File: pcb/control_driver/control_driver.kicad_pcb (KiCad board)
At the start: 2 copper layers, 60 parts, among them P1 CONN_2, P2 CONN_4, P3 CONN_2, P4 CONN_4, P5 CONN_4, P6 CONN_4, P7 CONN_4, Q1 MOSFET_N, Q2 MOSFET_N, Q3 MOSFET_N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

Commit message: control/driver PCB arranged
All the components for the control/driver PCB have
been arranged.  Next traces need to be added.
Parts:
- moved P7 485.1 mm to (251.5, 203.2)
- moved P6 462.2 mm to (231.1, 203.2)
- moved P1 461.5 mm to (266.7, 203.8), turned to 270 degrees
- moved D7 420.9 mm to (261.6, 179.1), turned to 90 degrees
- moved P5 417.0 mm to (204.5, 202.6), turned to 0 degrees
- moved R15 412.4 mm to (262.9, 189.2)
- moved R16 410.4 mm to (255.9, 180.3), turned to 270 degrees
- moved U8 396.6 mm to (246.4, 192.4)
- moved P3 379.1 mm to (196.8, 141.6), turned to 270 degrees
- moved U3 371.0 mm to (177.8, 192.4)
- moved R17 370.4 mm to (228.6, 189.2), turned to 90 degrees
- moved R13 356.5 mm to (251.5, 189.2), turned to 90 degrees
- moved R4 346.6 mm to (175.3, 180.3), turned to 270 degrees
- moved R11 337.1 mm to (240.0, 189.2), turned to 90 degrees
- moved D1 336.7 mm to (181.0, 179.1), turned to 90 degrees
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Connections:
- P2 pad 1: /control/CE0 -> /control/MOSI
- P2 pad 2: /control/SCLK -> /control/MISO
- P2 pad 3: /control/MOSI -> /control/SCLK
- P2 pad 4: (no net) -> /control/CE0
- P4 pad 1: /driver_4/DRV_B -> /driver_1/DRV_B
- P4 pad 2: /driver_3/DRV_B -> /driver_2/DRV_B
- P4 pad 3: /driver_2/DRV_B -> /driver_3/DRV_B
- P4 pad 4: /driver_1/DRV_B -> /driver_4/DRV_B
- P5 pad 1: /driver_8/DRV_B -> /driver_5/DRV_B
- P5 pad 2: /driver_7/DRV_B -> /driver_6/DRV_B
- P5 pad 3: /driver_6/DRV_B -> /driver_7/DRV_B
- P5 pad 4: /driver_5/DRV_B -> /driver_8/DRV_B
- U1 pad 12: N-0000033 (its old number) -> /control/MISO
- U2 pad 3: N-0000033 (its old number) -> /control/MISO

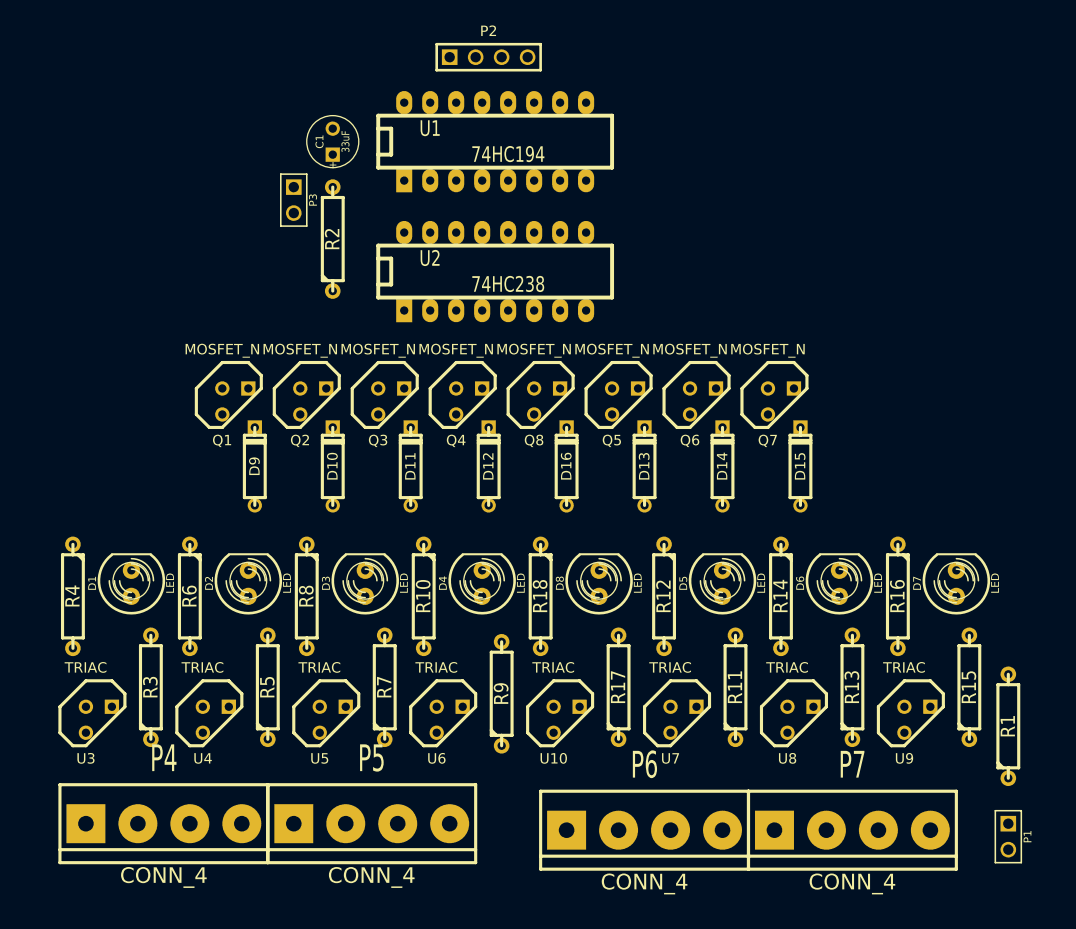
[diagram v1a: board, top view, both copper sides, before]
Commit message: completely connected control/driver PCB
A completely connected control/driver PCB has
been accomplished.  It could still be cleaned
up a bit.
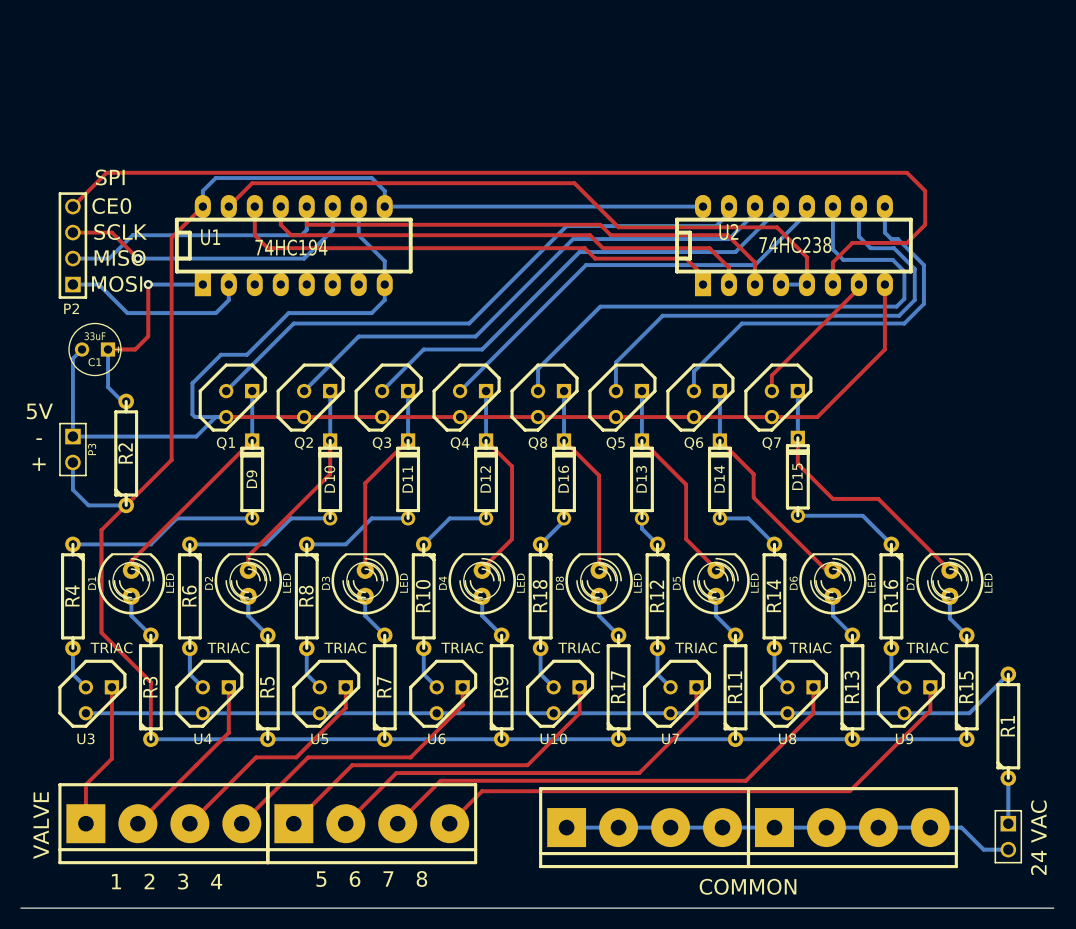
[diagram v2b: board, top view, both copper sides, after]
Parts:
- moved P2 44.6 mm to (175.3, 146.1), turned to 90 degrees
- moved P3 32.6 mm to (175.3, 166.0)
- moved C1 30.9 mm to (177.4, 156.2), turned to 180 degrees
- moved U2 29.3 mm to (245.7, 146.1)
- moved R2 29.1 mm to (180.5, 166.4)
- moved U1 22.2 mm to (196.8, 146.1)
- moved U10 1.91 mm to (223.5, 190.5)
- moved U3 1.91 mm to (177.8, 190.5)
- moved U4 1.91 mm to (189.2, 190.5)
- moved U5 1.91 mm to (200.7, 190.5)
- moved U6 1.91 mm to (212.1, 190.5)
- moved U7 1.91 mm to (234.9, 190.5)
- moved U8 1.91 mm to (246.4, 190.5)
- moved U9 1.91 mm to (257.8, 190.5)
- moved D12 1.30 mm to (215.6, 168.9)
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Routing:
- net +5V: track 0.00 -> 198.8 mm
- net GND: track 0.00 -> 136.9 mm
- net /control/CE0: track 0.00 -> 101.4 mm
- net /driver_1/DRV_A: track 0.00 -> 91.7 mm
- net /control/MISO: track 0.00 -> 75.6 mm
- net N-0000032: track 0.00 -> 65.7 mm
- net /driver_1/CTL: track 0.00 -> 57.0 mm
- net /driver_5/CTL: track 0.00 -> 55.6 mm
- net /driver_8/DRV_B: track 0.00 -> 53.9 mm
- net /driver_2/CTL: track 0.00 -> 51.9 mm
- net N-0000034: track 0.00 -> 49.1 mm
- net N-0000033: track 0.00 -> 49.0 mm
- net /driver_7/DRV_B: track 0.00 -> 47.7 mm
- net /driver_6/CTL: track 0.00 -> 47.3 mm
- net /driver_3/CTL: track 0.00 -> 46.5 mm
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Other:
- net class 0.5A added: clearance 0.254, trace_width 0.254, via_dia 0.889, via_drill 0.635
- net class 1.2A added: clearance 0.381, trace_width 0.381, via_dia 0.889, via_drill 0.635
- net class 1A added: clearance 0.3048, trace_width 0.3048, via_dia 0.889, via_drill 0.635
- board text added: "+"
- board text added: "-"
- board text added: "1 2 3 4"
- board text added: "24 VAC"
- board text added: "5 6 7 8"
- board text added: "5V"
- board text added: "CE0"
- board text added: "COMMON"
- board text added: "MISO"
- board text added: "MOSI"
- board text added: "SCLK"
- board text added: "SPI"
- board text added: "VALVE"

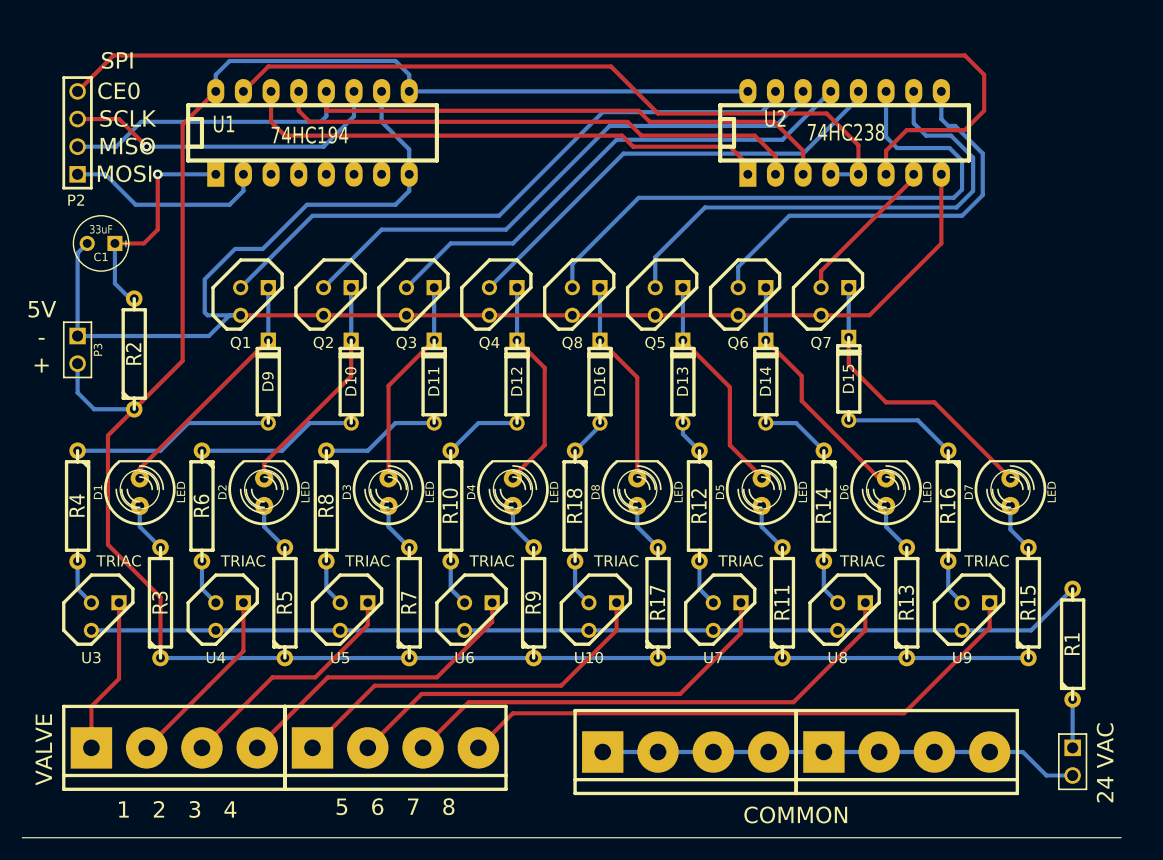
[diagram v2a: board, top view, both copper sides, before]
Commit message: cleaned up control/driver PCB
Rearranged wires and components to try and
minimize the PCB size.  Got it down to a ~3x4.
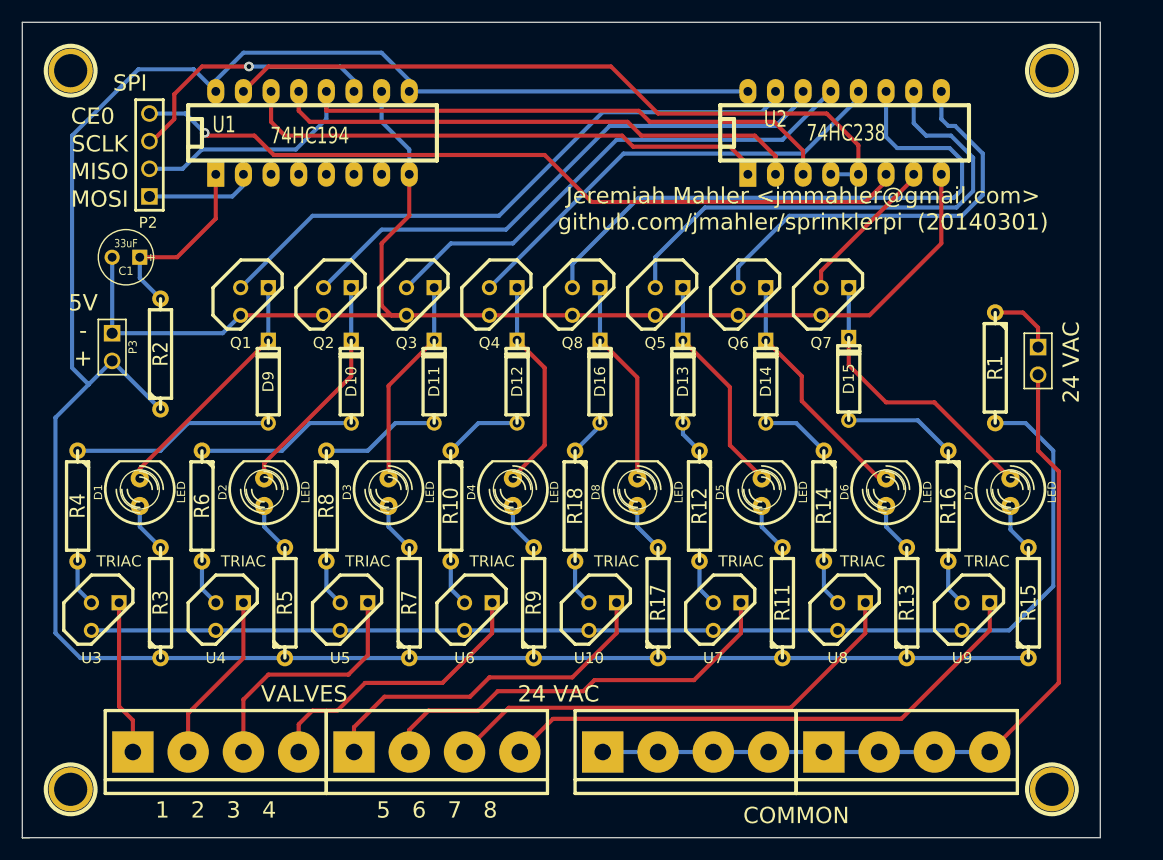
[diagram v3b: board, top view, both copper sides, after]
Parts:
- added 1PIN: P***, 1pin, F.Cu at (174.6, 140.3)
- added 1PIN: P***, 1pin, F.Cu at (264.8, 140.3)
- added 1PIN: P***, 1pin, F.Cu at (264.8, 206.4)
- added 1PIN: P***, 1pin, F.Cu at (174.6, 206.4)
- moved P1 37.0 mm to (263.5, 167.0)
- moved R1 26.4 mm to (259.6, 167.6), turned to 270 degrees
- moved P2 6.91 mm to (181.9, 148.1)
- moved P4 3.83 mm to (188.0, 202.9)
- moved P5 3.83 mm to (208.3, 202.9)
- moved P3 3.19 mm to (178.4, 165.7)
- moved C1 2.62 mm to (179.7, 157.5)
- moved R2 2.41 mm to (182.9, 166.4)
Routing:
- net N-0000014: track 44.1 -> 73.7 mm
- net /control/CE0: track 101.4 -> 72.5 mm, vias 0 -> 1
- net GND: track 136.9 -> 117.4 mm
- net +5V: track 198.8 -> 216.3 mm
- net /driver_1/DRV_A: track 91.7 -> 108.9 mm
- net /control/MOSI: track 18.4 -> 10.1 mm
- net /control/MISO: track 75.6 -> 70.0 mm
- net /control/SCLK: track 29.9 -> 24.5 mm
- net N-0000031: track 20.9 -> 17.1 mm, vias 1 -> 0
- net /driver_8/DRV_B: track 53.9 -> 50.3 mm
- net /driver_7/DRV_B: track 47.7 -> 44.1 mm
- net /driver_6/DRV_B: track 41.5 -> 39.0 mm
- net /driver_5/DRV_B: track 35.0 -> 32.8 mm
- net N-000001: track 4.44 -> 6.29 mm
- net /driver_4/DRV_B: track 28.2 -> 26.6 mm
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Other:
- board outline added: 99.1 x 74.9 mm
- board text added: "Jeremiah Mahler <jmmahler@gmail.com> github.com/jmahler/sprinklerpi (20140301)"
- board text added: "VALVES"
- board text removed: "VALVE"
